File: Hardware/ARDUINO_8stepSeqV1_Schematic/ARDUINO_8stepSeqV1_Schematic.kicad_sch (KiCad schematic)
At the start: 12 parts, among them SW1 SW_Push, SW10 SW_Push, SW11 SW_Push, SW2 SW_Push, SW3 SW_Push, SW4 SW_Push, SW5 SW_Push, SW6 SW_Push, SW7 SW_Push, SW8 SW_Push, SW9 SW_Push

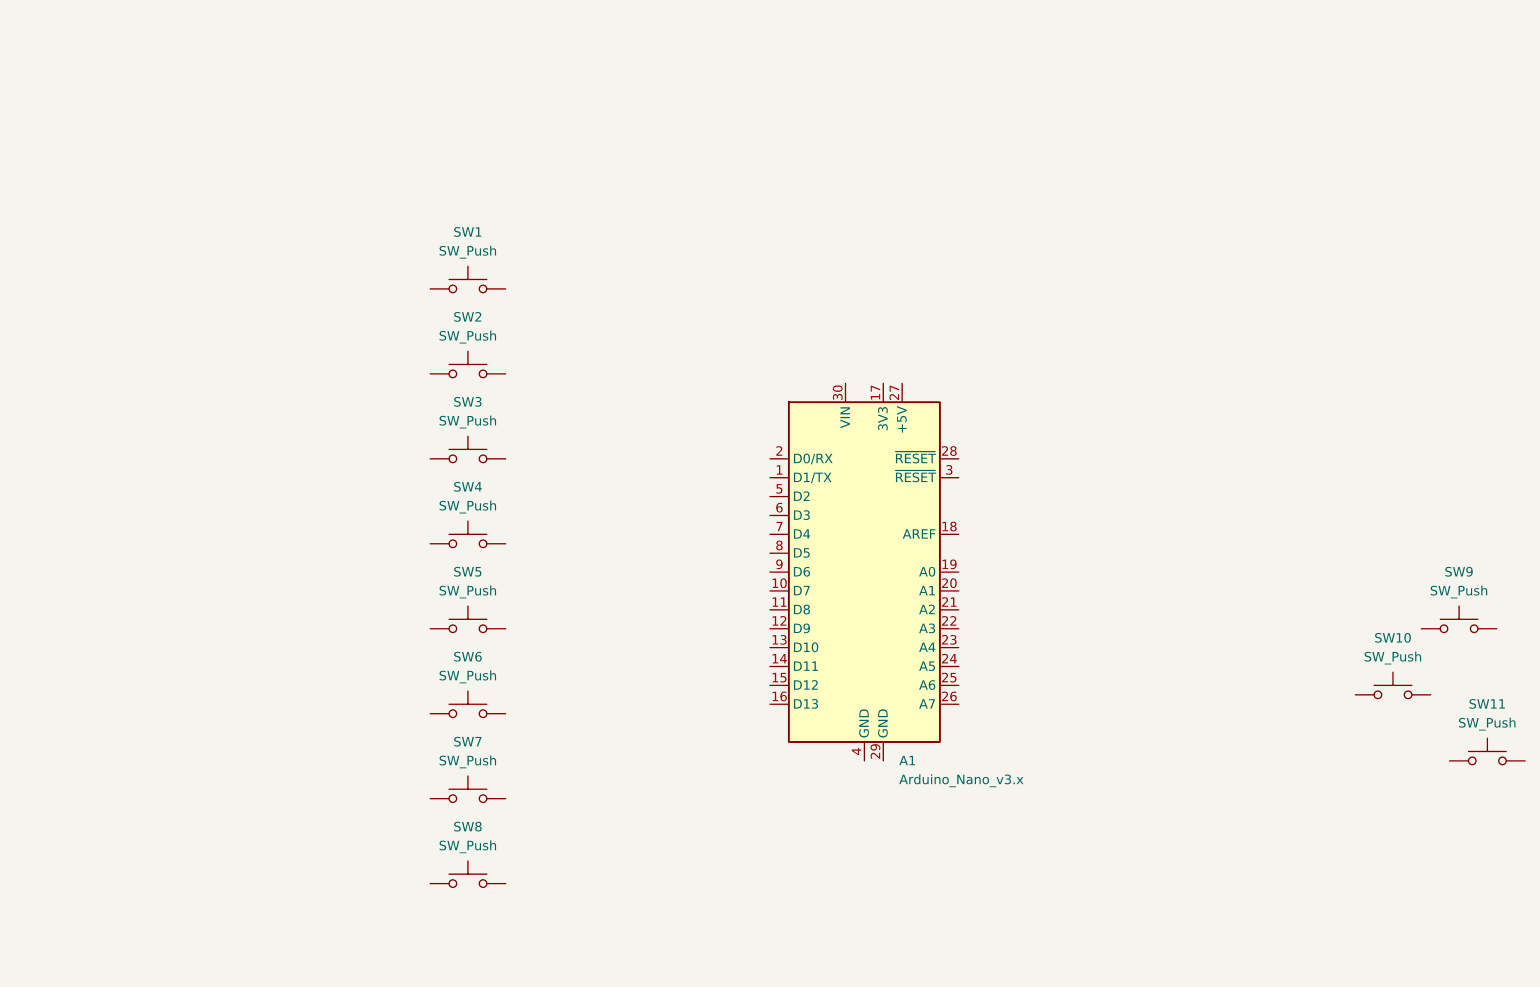
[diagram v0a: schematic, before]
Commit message: ARDUINO_8steoSeq | Hardware Layout Modified
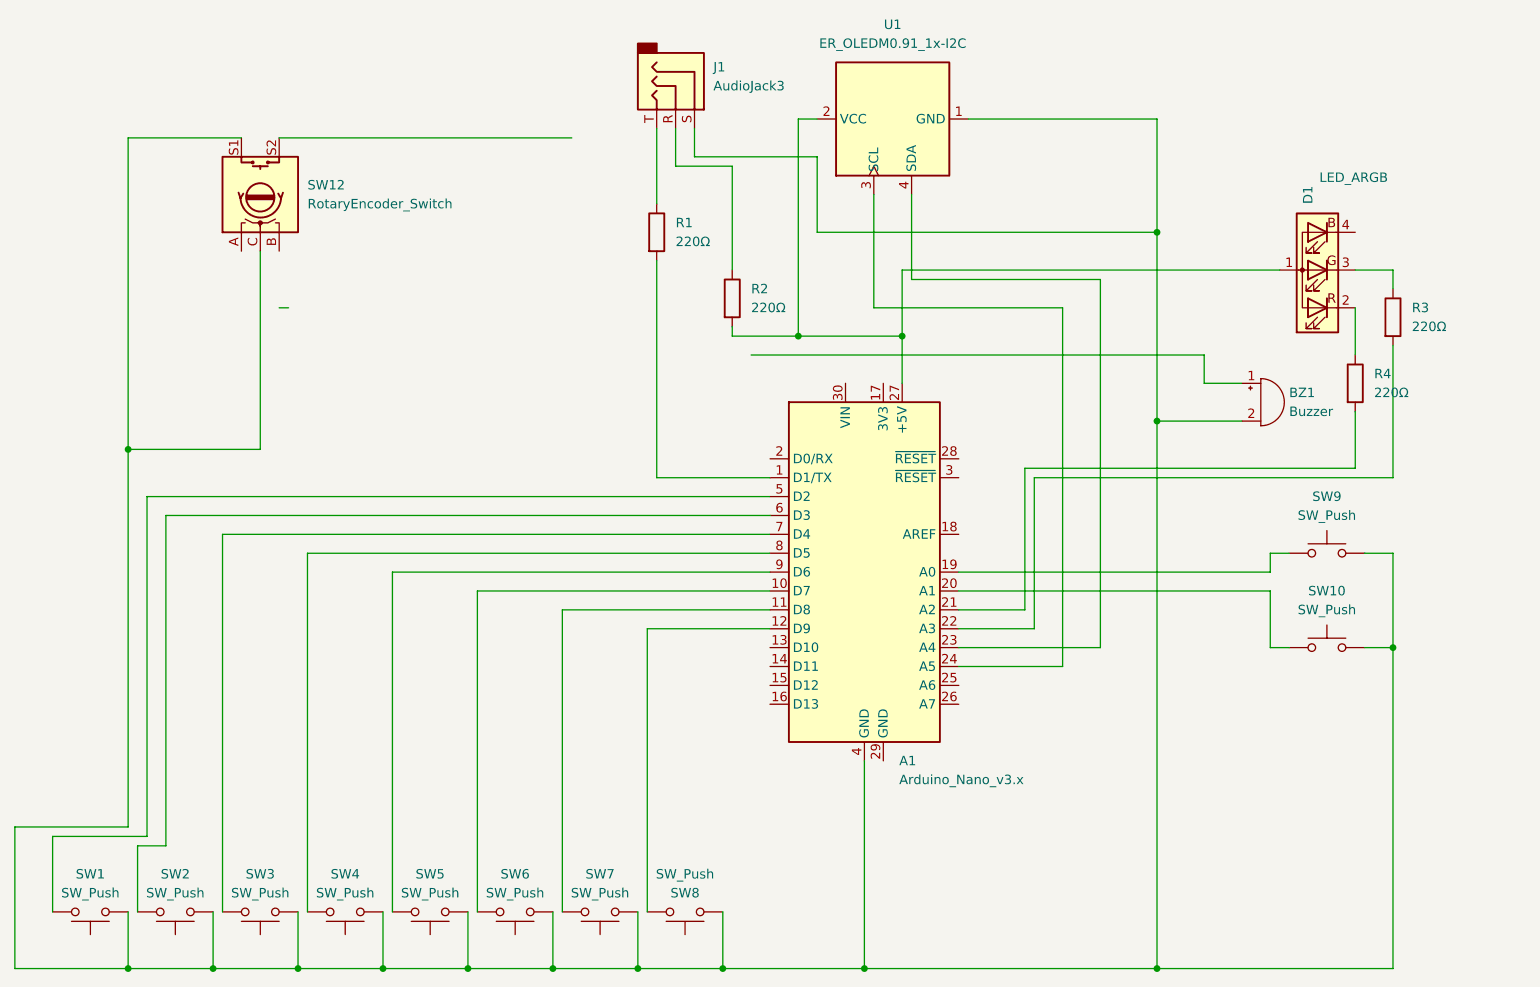
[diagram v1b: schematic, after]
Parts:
- removed SW11: SW_Push, symbol Switch:SW_Push
- added BZ1: Buzzer, symbol Device:Buzzer
- added D1: LED_ARGB, symbol Device:LED_ARGB
- added J1: AudioJack3, symbol Connector_Audio:AudioJack3
- added R1, R2, R3, R4: 220Ω, symbol Device:R
- added SW12: RotaryEncoder_Switch, symbol Device:RotaryEncoder_Switch
- added U1: ER_OLEDM0.91_1x-I2C, Display:ER_OLEDM0.91_1x-I2C, symbol Display_Graphic:ER_OLEDM0.91_1x-I2C
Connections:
- net at SW9.1: now also A1.19 (A0)
- net at SW9.2: now also A1.4 (GND), SW1.1, SW10.2, SW2.1, SW3.1, SW4.1, SW5.1, SW6.1, SW7.1, SW8.1, BZ1.2 (-), J1.S, SW12.C, SW12.S1, U1.1 (GND)
- net at SW7.2: now also A1.11 (D8)
- net at SW8.2: now also A1.12 (D9)
- net at SW1.2: now also A1.5 (D2)
- net at A1.1 (D1/TX): now also R1.2
- net at A1.10 (D7): now also SW6.2
- net at A1.20 (A1): now also SW10.1
- net at A1.21 (A2): now also R4.2
- net at A1.22 (A3): now also R3.2
- net at A1.23 (A4): now also U1.4 (SDA)
- net at A1.24 (A5): now also U1.3 (SCL)
- net at A1.27 (+5V): now also D1.1 (A), R2.2, U1.2 (VCC)
- net at A1.6 (D3): now also SW2.2
- net at A1.7 (D4): now also SW3.2
- net at A1.8 (D5): now also SW4.2
- net at A1.9 (D6): now also SW5.2
- new net: D1.2 (RK), R4.1
- new net: D1.3 (GK), R3.1
- new net: J1.R, R2.1
- new net: J1.T, R1.1
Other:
- moved on the sheet: SW1, SW10, SW2, SW3, SW4, SW5, SW6, SW7, SW8, SW9

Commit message: ARDUINO_8steoSeq | Hardware revision
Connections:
- net at A1.4 (GND), BZ1.2 (-), J1.S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: no longer SW12.C
- net at BZ1.1 (+): now also A1.16 (D13)
- net at SW7.2: now also A1.14 (D11); no longer A1.11 (D8)
- net at A1.27 (+5V), D1.1 (A), R2.2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: now also SW12.C
- net at D1.2 (RK): now also R3.1; no longer R4.1
- net at D1.3 (GK): now also R4.1; no longer R3.1
- net at SW12.A: now also A1.6 (D3)
- net at SW12.B: now also A1.5 (D2)
- net at SW8.2: now also A1.15 (D12); no longer A1.12 (D9)
- net at SW1.2: now also A1.8 (D5); no longer A1.5 (D2)
- net at A1.10 (D7): now also SW3.2; no longer SW6.2
- net at A1.13 (D10): now also SW6.2
- net at SW2.2: now also A1.9 (D6); no longer A1.6 (D3)
- net at A1.7 (D4): no longer SW3.2
- net at SW4.2: now also A1.11 (D8); no longer A1.8 (D5)
- net at SW5.2: now also A1.12 (D9); no longer A1.9 (D6)
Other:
- moved on the sheet: D1
